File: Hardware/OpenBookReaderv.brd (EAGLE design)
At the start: 170.2 x 111.2 mm, 103 parts, among them IC1 BD5229G-TR, IC4 XC6220A331MR-G, J1 FH34SRJ-24S-0.5SH_99_, J2 SAMACSYS_PARTS_USB4110-GF-A, J3 QWIIC_RIGHT_ANGLE, J4 112A-TAAR-R03_ATTEND, Q1 20V/4.2A/52mΩ/1.4W, Q2 20V/4.2A/52mΩ/1.4W, Q3 SI1308EDL-T1-GE3, U1 W25Q512JVEIQ, U2 ESP32-C6-WROOM-1-N8, U3 DS3231SN#, U4 MAX17048G+T10

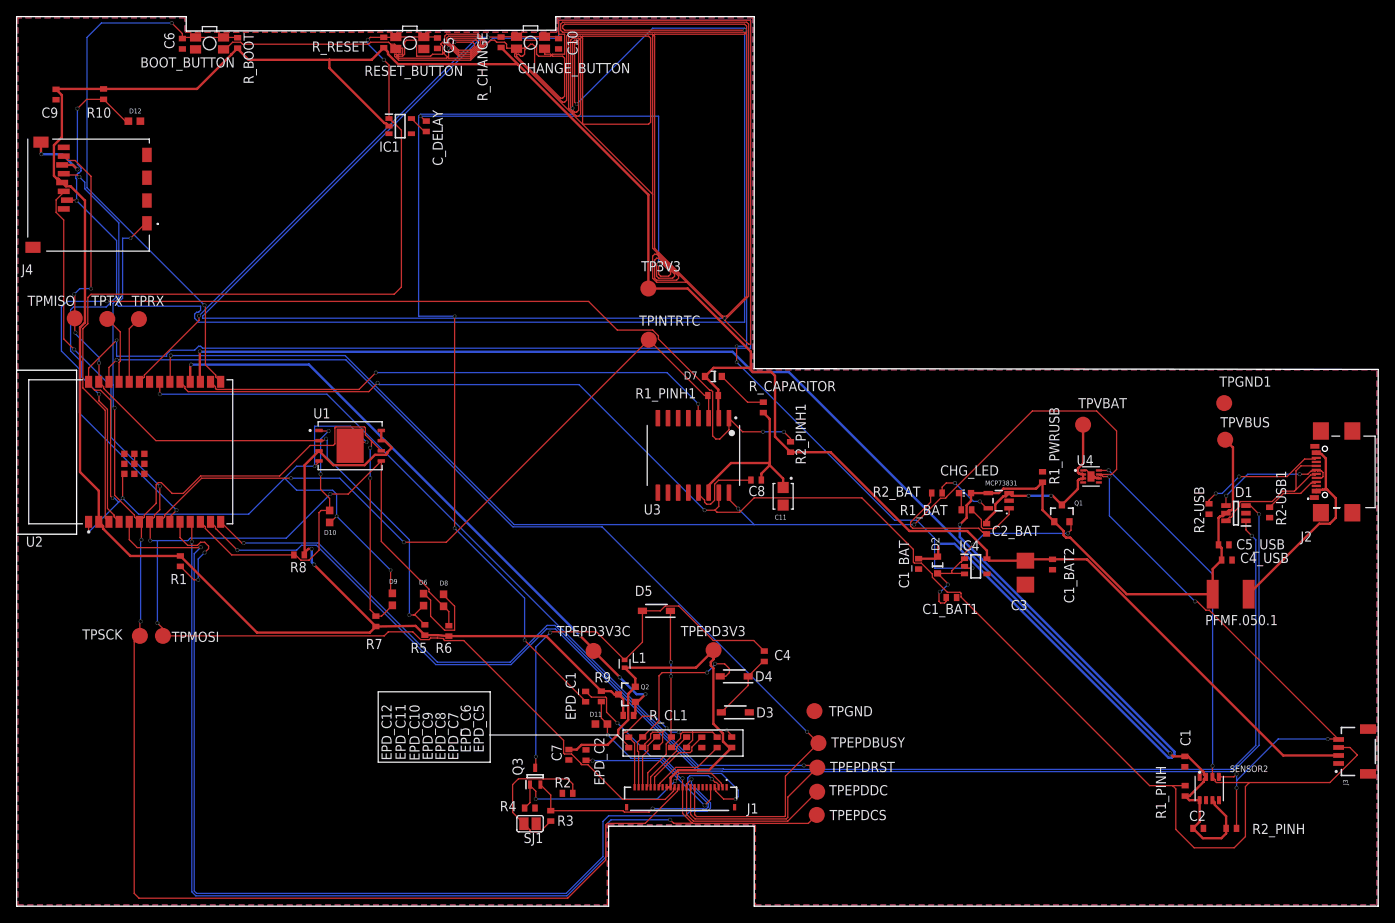
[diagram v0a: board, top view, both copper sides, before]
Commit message: GND layers hole and esp32 component cut fixed
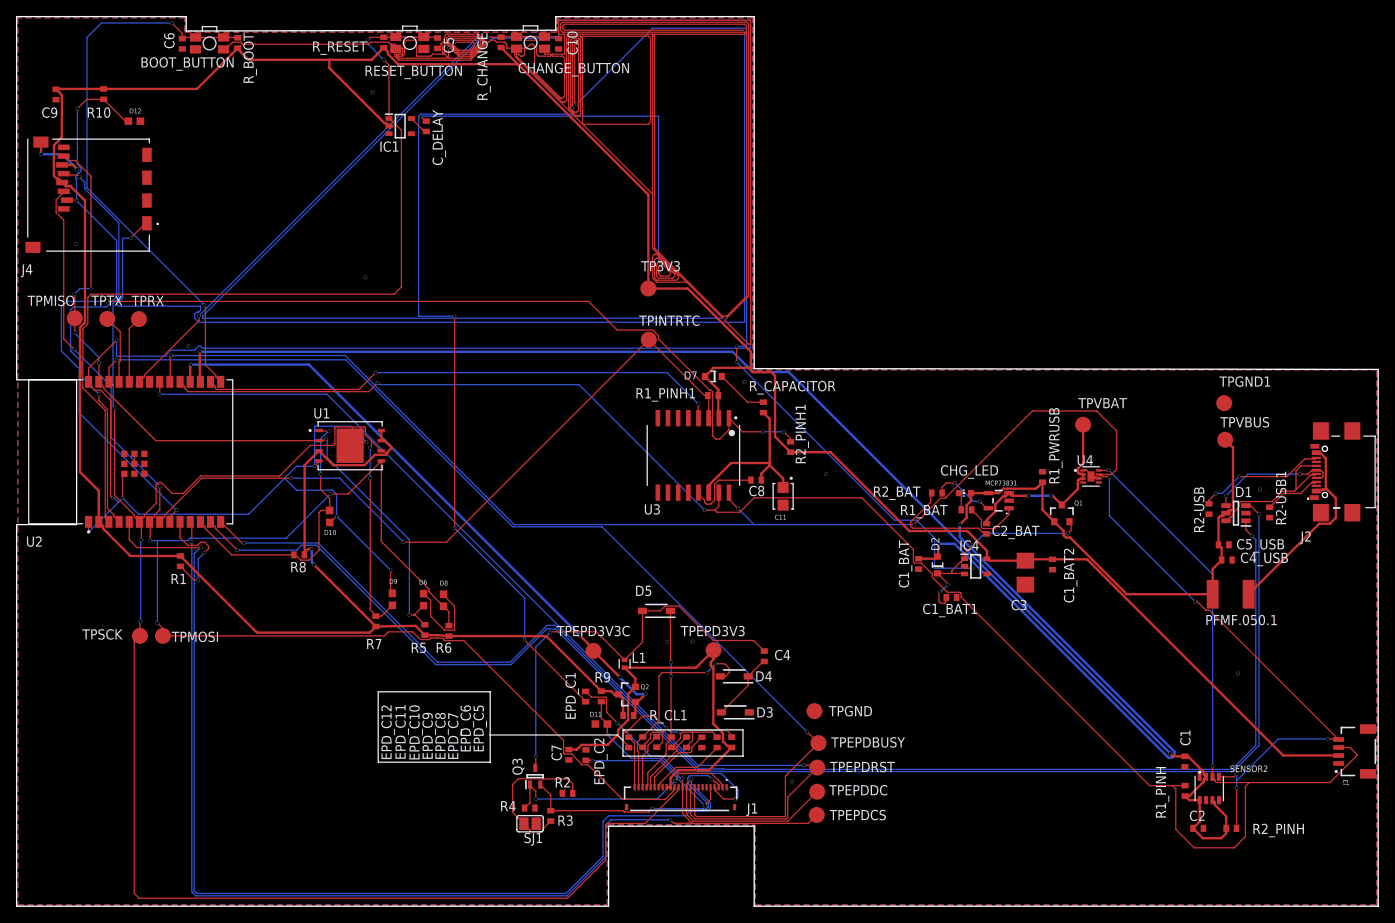
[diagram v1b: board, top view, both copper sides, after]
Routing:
- net GND: vias 29 -> 40
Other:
- outline, holes or cut-outs redrawn

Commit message: Removed via stitching and added a new gnd layer
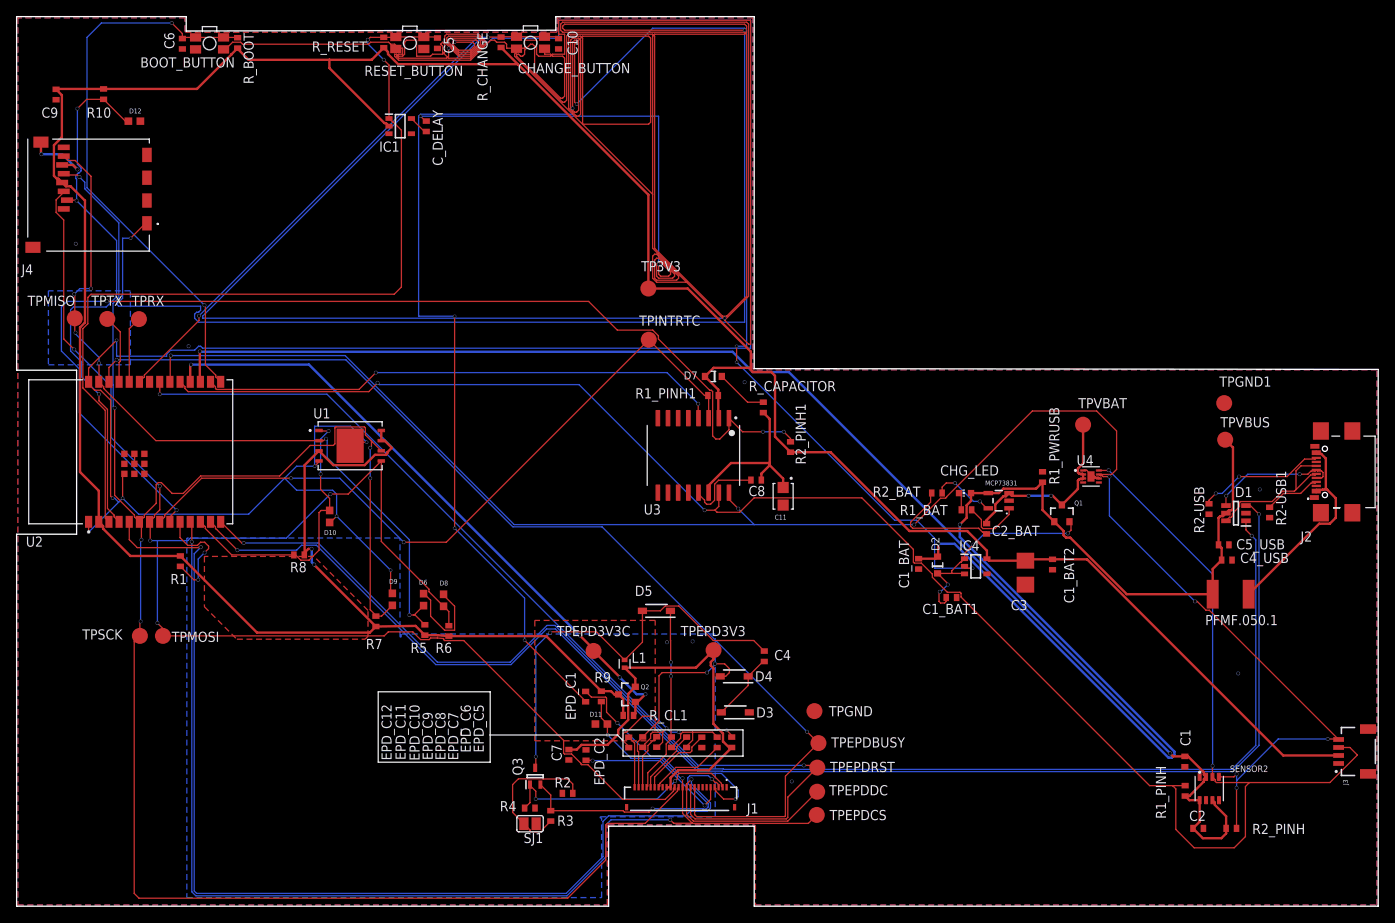
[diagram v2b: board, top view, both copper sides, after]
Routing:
- net GND: vias 40 -> 37
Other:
- outline, holes or cut-outs redrawn
